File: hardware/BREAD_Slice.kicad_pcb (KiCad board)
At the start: 2 copper layers, 72.6 x 100 mm, 16 parts, among them J1 Conn_01x10_Female, J2 I2C_01x04

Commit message: Initial commit
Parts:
- removed C3, C4: 22uF, Capacitor_SMD:C_1206_3216Metric
- removed D1: WS2812B_5050, SparkFun-LED:WS2812-5050-4PIN
- removed HS1: Heatsink_Pad, SparkFun-Fuse:Thermal Pad
- removed J2: I2C_01x04, Connector_JST:JST_SH_SM04B-SRSS-TB_1x04-1MP_P1.00mm_Horizontal
- removed L1: 4.7uH, Inductor_SMD:L_1210_3225Metric
- removed U1: ~, Package_TO_SOT_SMD:TSOT-23-6
- C1: value 22uF -> 10uF_t; footprint Capacitor_SMD:C_1206_3216Metric -> OCI_UPL_FOOTPRINTS:C_2312
- C2: value 100nF -> 10uF_t; footprint Capacitor_SMD:C_1206_3216Metric -> OCI_UPL_FOOTPRINTS:C_2312
- H1, H4: footprint MountingHole:MountingHole_5mm -> MountingHole:MountingHole_3.2mm_M3_DIN965_Pad
- H2: renamed from H3; footprint MountingHole:MountingHole_5mm -> MountingHole:MountingHole_3.2mm_M3_DIN965_Pad
- H3: renamed from H2; footprint MountingHole:MountingHole_5mm -> MountingHole:MountingHole_3.2mm_M3_DIN965_Pad
- moved Logo1 77.4 mm to (171.3, 135.4), turned to 0 degrees
- moved C1 34.0 mm to (156.4, 100.0), turned to 0 degrees
- moved C2 31.4 mm to (156.4, 107.7), turned to 0 degrees
- moved A1 7.59 mm to (135.0, 100.0)
- moved J1 3.43 mm to (129.6, 78.8)
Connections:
- A1 pad 10: unconnected-(A1-D7-Pad10) -> /BR2
- A1 pad 11: unconnected-(A1-D8-Pad11) -> /THRM2
- A1 pad 12: unconnected-(A1-D9-Pad12) -> /DIR1
- A1 pad 13: unconnected-(A1-D10-Pad13) -> /MC1
- A1 pad 14: unconnected-(A1-D11-Pad14) -> /BR1
- A1 pad 15: unconnected-(A1-D12-Pad15) -> /THRM1
- A1 pad 19: unconnected-(A1-A0-Pad19) -> /A1
- A1 pad 20: unconnected-(A1-A1-Pad20) -> /B1
- A1 pad 21: unconnected-(A1-A2-Pad21) -> /A2
- A1 pad 22: unconnected-(A1-A3-Pad22) -> /B2
- A1 pad 25: unconnected-(A1-A6-Pad25) -> /CSEN1
- A1 pad 26: unconnected-(A1-A7-Pad26) -> /CSEN2
- A1 pad 30: unconnected-(A1-VIN-Pad30) -> +12V
- A1 pad 8: /LED -> /DIR2
- A1 pad 9: unconnected-(A1-D6-Pad9) -> /MC2
- C1 pad 1: GND -> +12V
- C1 pad 2: +12V -> GND
- C2 pad 1: Net-(U1-SW) -> +5V
- C2 pad 2: Net-(U1-BST) -> GND
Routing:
- net +5V: track 108.9 -> 3.60 mm, vias 1 -> 0
- net /LED: track 51.5 -> 0.00 mm
- net /I2C_CLK: track 78.5 -> 39.9 mm, vias 2 -> 1
- net /I2C_DAT: track 76.6 -> 39.9 mm, vias 2 -> 1
- net GND: track 19.6 -> 0.00 mm, vias 14 -> 0
- net /E_STOP: track 30.1 -> 20.9 mm
- net /INT: track 28.8 -> 20.9 mm
- net /SYNC: track 27.9 -> 20.9 mm
- net Net-(U1-SW): track 5.22 -> 0.00 mm
- net Net-(U1-BST): track 2.64 -> 0.00 mm
- net +12V: track 46.8 -> 45.5 mm
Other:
- board size 72.6 x 100 mm -> 70 x 100 mm
- board text added: "<Description> SLC_TEMP R<version#> year"
- board text removed: "12V->5V Reg"
- board text removed: "5V I2C Connector"
- board text removed: "BREAD Slice Template SLC_TEMP <version> <year>"
- board text removed: "LED"

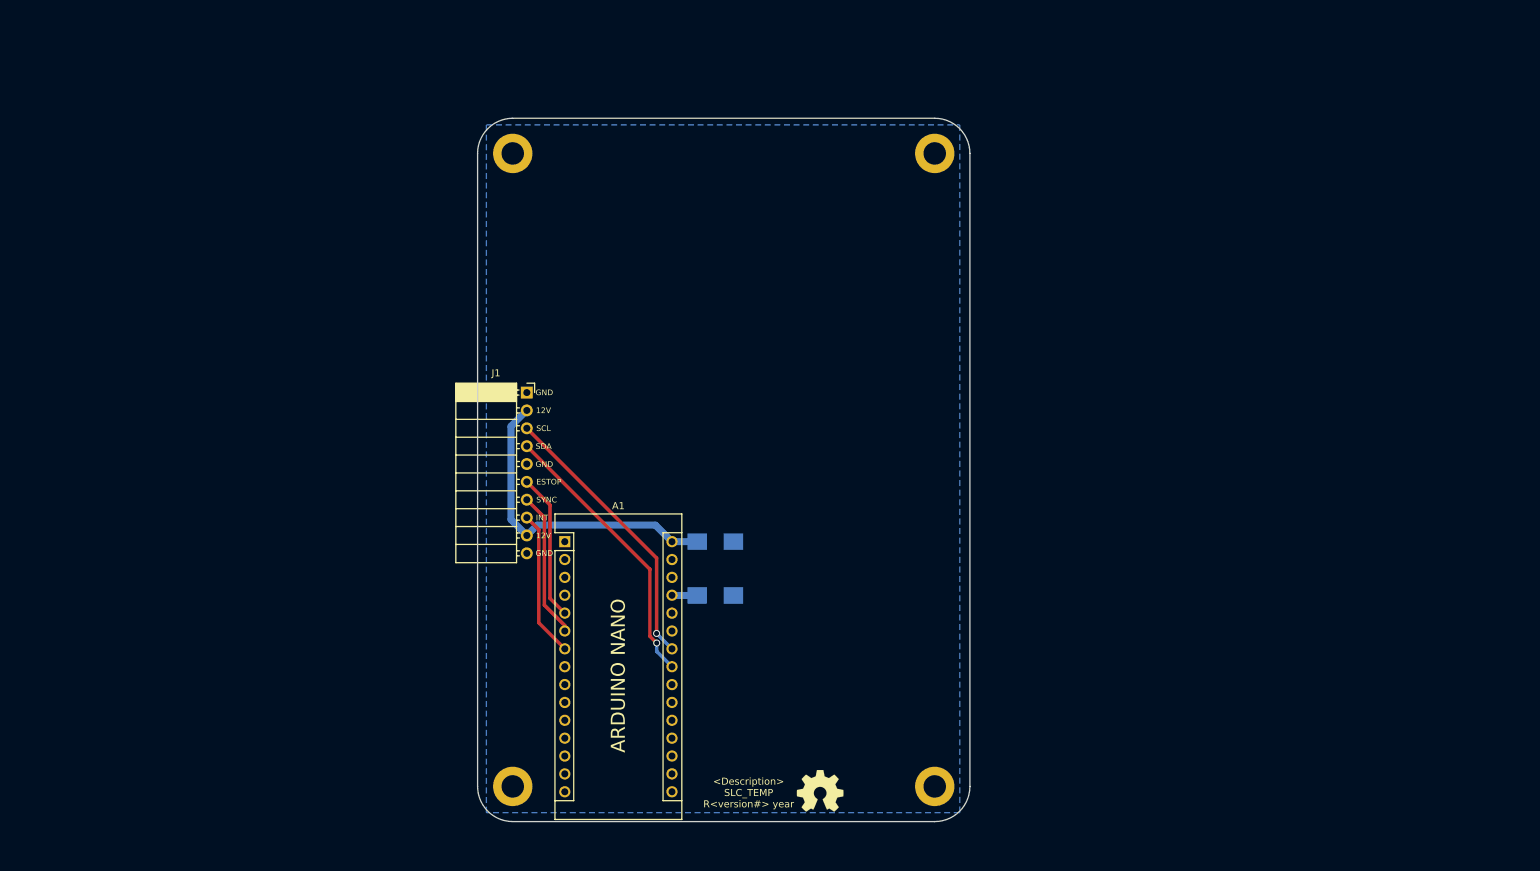
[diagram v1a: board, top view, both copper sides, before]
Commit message: initial layout poisitions done
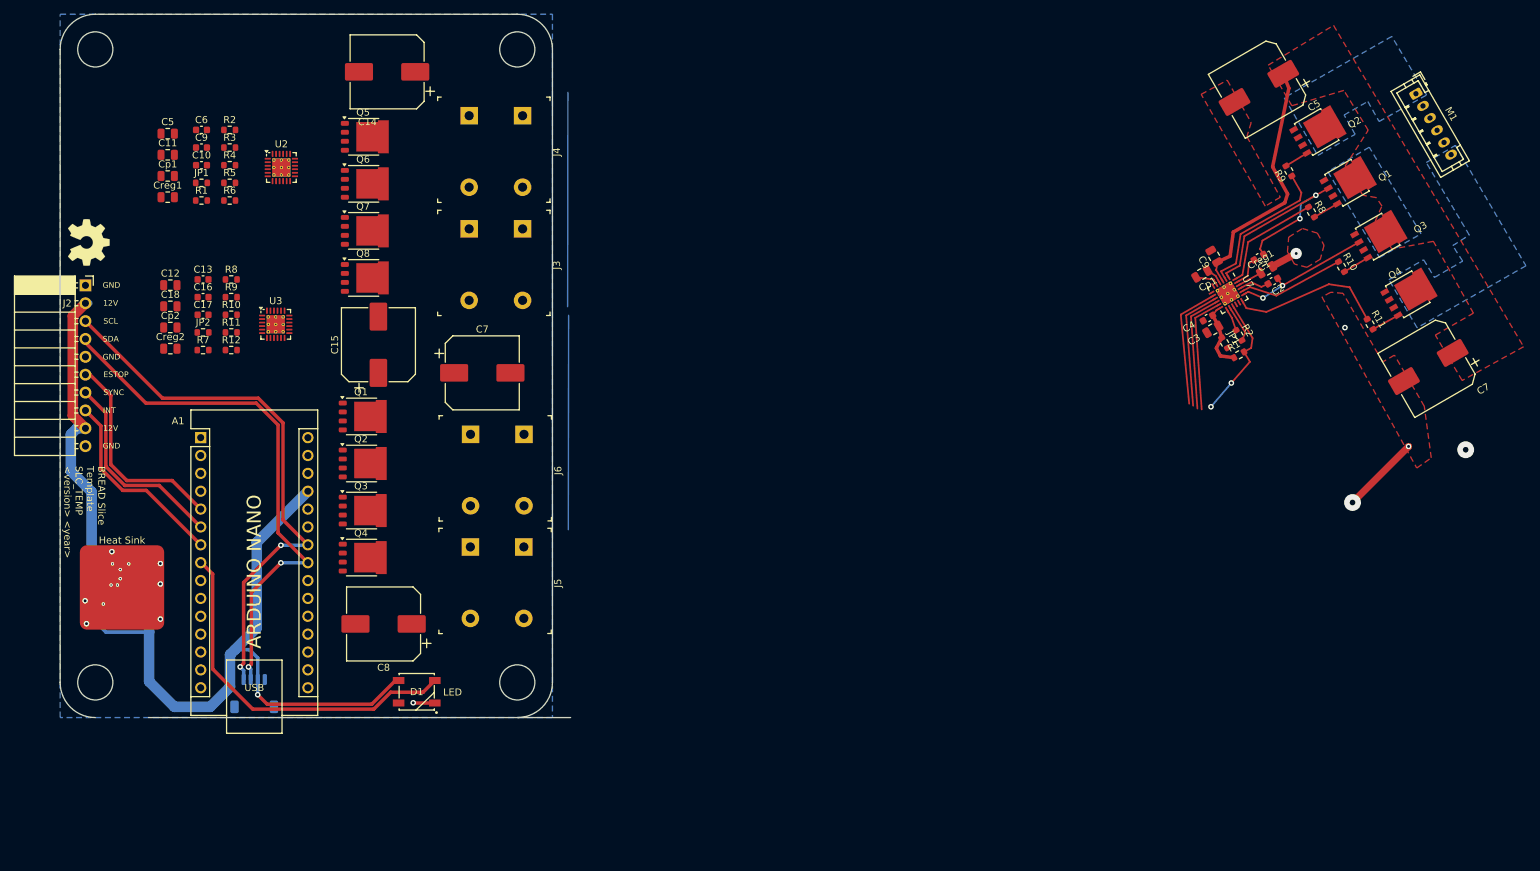
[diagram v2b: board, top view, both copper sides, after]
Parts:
- removed the C1 at (156.4, 100.0)
- removed the C2 at (156.4, 107.7)
- added C1: 10n, Capacitor_SMD:C_0603_1608Metric, F.Cu at (233.7, 59.6)
- added C1: 22uF, Capacitor_SMD:C_1206_3216Metric, B.Cu at (69.2, 104.7)
- added C10: 1n, Capacitor_SMD:C_0603_1608Metric, F.Cu at (83.3, 46.5)
- added C11: 50V 10U, Capacitor_SMD:C_0805_2012Metric, F.Cu at (78.5, 45.0)
- added C12: 10U, Capacitor_SMD:C_0805_2012Metric, F.Cu at (78.9, 63.5)
- added C13: 100N, Capacitor_SMD:C_0603_1608Metric, F.Cu at (83.6, 62.7)
- added C14: 50V 220U, Capacitor_SMD:CP_Elec_10x10, F.Cu at (109.7, 33.2)
- added C15: 50V 220U, Capacitor_SMD:CP_Elec_10x10, F.Cu at (108.5, 72.0)
- added C16: 1n, Capacitor_SMD:C_0603_1608Metric, F.Cu at (83.6, 65.2)
- added C17: 1n, Capacitor_SMD:C_0603_1608Metric, F.Cu at (83.6, 67.7)
- added C18: 50V 10U, Capacitor_SMD:C_0805_2012Metric, F.Cu at (78.9, 66.5)
- added C2: 10n, Capacitor_SMD:C_0603_1608Metric, F.Cu at (235.7, 63.0)
- added C2: 100nF, Capacitor_SMD:C_1206_3216Metric, B.Cu at (71.8, 111.5)
- added C3: 10U, Capacitor_SMD:C_0805_2012Metric, F.Cu at (227.1, 69.8)
- added C3: 22uF, Capacitor_SMD:C_1206_3216Metric, B.Cu at (74.5, 104.7)
- added C4: 100N, Capacitor_SMD:C_0603_1608Metric, F.Cu at (226.4, 68.2)
- added C4: 22uF, Capacitor_SMD:C_1206_3216Metric, B.Cu at (74.5, 101.7)
- added C5: 50V 220U, Capacitor_SMD:CP_Elec_10x10, F.Cu at (233.7, 35.5)
- added C5: 10U, Capacitor_SMD:C_0805_2012Metric, F.Cu at (78.5, 42.0)
- added C6: 100N, Capacitor_SMD:C_0603_1608Metric, F.Cu at (83.3, 41.5)
- added C7: 50V 220U, Capacitor_SMD:CP_Elec_10x10, F.Cu at (123.3, 76.0)
- added C7: 50V 220U, Capacitor_SMD:CP_Elec_10x10, F.Cu at (257.8, 75.2)
- added C8: 50V 220U, Capacitor_SMD:CP_Elec_10x10, F.Cu at (109.2, 111.7)
- added C9: 50V 10U, Capacitor_SMD:C_0805_2012Metric, F.Cu at (227.3, 59.4)
- added C9: 1n, Capacitor_SMD:C_0603_1608Metric, F.Cu at (83.3, 44.0)
- added Cp1: 16V 470n, Capacitor_SMD:C_0805_2012Metric, F.Cu at (225.6, 61.9)
- added Cp1: 16V 470n, Capacitor_SMD:C_0805_2012Metric, F.Cu at (78.5, 48.0)
- added Cp2: 16V 470n, Capacitor_SMD:C_0805_2012Metric, F.Cu at (78.9, 69.5)
- added Creg1: 16V 22u, Capacitor_SMD:C_0805_2012Metric, F.Cu at (234.8, 61.3)
- added Creg1: 16V 22u, Capacitor_SMD:C_0805_2012Metric, F.Cu at (78.5, 51.0)
- added Creg2: 16V 22u, Capacitor_SMD:C_0805_2012Metric, F.Cu at (78.9, 72.6)
- added D1: WS2812B_5050, SparkFun-LED:WS2812-5050-4PIN, F.Cu at (113.9, 121.3)
- added HS1: Heatsink_Pad, KML-Custom:Thermal Pad, F.Cu at (72.0, 106.5)
- added J1: I2C_01x04, Connector_JST:JST_SH_SM04B-SRSS-TB_1x04-1MP_P1.00mm_Horizontal, B.Cu at (90.8, 121.6)
- added J3: Conn_01x02_Socket, Library:Term_Block_1x2_P10.16mm, F.Cu at (129.0, 55.5)
- added J4: Conn_01x02_Socket, Library:Term_Block_1x2_P10.16mm, F.Cu at (129.0, 39.4)
- added J5: Conn_01x02_Socket, Library:Term_Block_1x2_P10.16mm, F.Cu at (129.2, 100.8)
- added J6: Conn_01x02_Socket, Library:Term_Block_1x2_P10.16mm, F.Cu at (129.2, 84.7)
- added JP1: Jumper_2_Open, Resistor_SMD:R_0603_1608Metric, F.Cu at (83.3, 49.0)
- added JP1: Jumper_2_Open, Resistor_SMD:R_0603_1608Metric, F.Cu at (228.8, 71.7)
- added JP2: Jumper_2_Open, Resistor_SMD:R_0603_1608Metric, F.Cu at (83.6, 70.2)
- added L1: 4.7uH, Inductor_SMD:L_1210_3225Metric, B.Cu at (74.5, 108.0)
- added M1: Motor_2BitEncoder, Connector_JST:JST_PH_B6B-PH-K_1x06_P2.00mm_Vertical, F.Cu at (256.0, 36.3)
- added Q1: PSMN1R0-30YLC,115, Package_TO_SOT_SMD:LFPAK56, F.Cu at (106.1, 82.2)
- added Q1: PSMN1R0-30YLC,115, Package_TO_SOT_SMD:LFPAK56, F.Cu at (246.2, 49.0)
- added Q2: PSMN1R0-30YLC,115, Package_TO_SOT_SMD:LFPAK56, F.Cu at (241.9, 41.8)
- added Q2: PSMN1R0-30YLC,115, Package_TO_SOT_SMD:LFPAK56, F.Cu at (106.1, 88.9)
- added Q3: PSMN1R0-30YLC,115, Package_TO_SOT_SMD:LFPAK56, F.Cu at (106.1, 95.6)
- added Q3: PSMN1R0-30YLC,115, Package_TO_SOT_SMD:LFPAK56, F.Cu at (250.6, 56.6)
- added Q4: PSMN1R0-30YLC,115, Package_TO_SOT_SMD:LFPAK56, F.Cu at (106.1, 102.3)
- added Q4: PSMN1R0-30YLC,115, Package_TO_SOT_SMD:LFPAK56, F.Cu at (254.9, 64.8)
- added Q5: PSMN1R0-30YLC,115, Package_TO_SOT_SMD:LFPAK56, F.Cu at (106.4, 42.4)
- added Q6: PSMN1R0-30YLC,115, Package_TO_SOT_SMD:LFPAK56, F.Cu at (106.4, 49.1)
- added Q7: PSMN1R0-30YLC,115, Package_TO_SOT_SMD:LFPAK56, F.Cu at (106.4, 55.8)
- added Q8: PSMN1R0-30YLC,115, Package_TO_SOT_SMD:LFPAK56, F.Cu at (106.4, 62.5)
- added R1: 10K, Resistor_SMD:R_0603_1608Metric, F.Cu at (230.9, 73.4)
- added R1: 10K, Resistor_SMD:R_0603_1608Metric, F.Cu at (83.3, 51.5)
- added R10: 1K, Resistor_SMD:R_0603_1608Metric, F.Cu at (87.6, 67.7)
- added R10: 1K, Resistor_SMD:R_0603_1608Metric, F.Cu at (245.4, 60.9)
- added R11: 1K, Resistor_SMD:R_0603_1608Metric, F.Cu at (249.5, 69.1)
- added R11: 1K, Resistor_SMD:R_0603_1608Metric, F.Cu at (87.6, 70.2)
- added R12: 10K, Resistor_SMD:R_0603_1608Metric, F.Cu at (87.6, 72.8)
- added R2: 1K, Resistor_SMD:R_0603_1608Metric, F.Cu at (87.4, 41.5)
- added R2: 10K, Resistor_SMD:R_0603_1608Metric, F.Cu at (230.9, 70.7)
- added R3: 1K, Resistor_SMD:R_0603_1608Metric, F.Cu at (87.4, 44.0)
- added R4: 1K, Resistor_SMD:R_0603_1608Metric, F.Cu at (87.4, 46.5)
- added R5: 1K, Resistor_SMD:R_0603_1608Metric, F.Cu at (87.4, 49.0)
- added R6: 10K, Resistor_SMD:R_0603_1608Metric, F.Cu at (87.4, 51.5)
- added R7: 10K, Resistor_SMD:R_0603_1608Metric, F.Cu at (83.6, 72.8)
- added R8: 1K, Resistor_SMD:R_0603_1608Metric, F.Cu at (241.2, 53.1)
- added R8: 1K, Resistor_SMD:R_0603_1608Metric, F.Cu at (87.6, 62.7)
- added R9: 1K, Resistor_SMD:R_0603_1608Metric, F.Cu at (87.6, 65.2)
- added R9: 1K, Resistor_SMD:R_0603_1608Metric, F.Cu at (238.0, 47.3)
- added U1: ~, Package_TO_SOT_SMD:TSOT-23-6, B.Cu at (69.4, 108.0)
- added U2: ~, Package_DFN_QFN:HVQFN-24-1EP_4x4mm_P0.5mm_EP2.6x2.6mm_ThermalVias, F.Cu at (94.7, 46.8)
- added U3: ~, Package_DFN_QFN:HVQFN-24-1EP_4x4mm_P0.5mm_EP2.6x2.6mm_ThermalVias, F.Cu at (93.9, 69.1)
- added U7: ~, Package_DFN_QFN:HVQFN-24-1EP_4x4mm_P0.5mm_EP2.6x2.6mm_ThermalVias, F.Cu at (229.3, 64.7)
- H1, H4: footprint MountingHole:MountingHole_3.2mm_M3_DIN965_Pad -> MountingHole:MountingHole_5mm
- H2: renamed from H3; footprint MountingHole:MountingHole_3.2mm_M3_DIN965_Pad -> MountingHole:MountingHole_5mm
- H3: renamed from H2; footprint MountingHole:MountingHole_3.2mm_M3_DIN965_Pad -> MountingHole:MountingHole_5mm
- moved Logo1 130.0 mm to (67.3, 57.4), turned to -90 degrees
- moved J2 64.6 mm to (66.8, 63.6)
- moved H1 61.2 mm to (68.2, 30.0)
- moved H2 61.2 mm to (68.2, 120.0)
- moved H3 61.2 mm to (128.2, 30.0)
- moved H4 61.2 mm to (128.2, 120.0)
- moved A1 53.8 mm to (83.2, 85.2)
- renumbered J1 to J2
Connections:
- A1 pad 10: /BR2 -> /BLO1
- A1 pad 11: /THRM2 -> /AHI1
- A1 pad 12: /DIR1 -> /ALO1
- A1 pad 13: /MC1 -> /BHI2
- A1 pad 14: /BR1 -> /BLO2
- A1 pad 15: /THRM1 -> /AHI2
- A1 pad 16: unconnected-(A1-Pad16) -> /ALO2
- A1 pad 19: /A1 -> /FAULT1
- A1 pad 20: /B1 -> /RESET1
- A1 pad 21: /A2 -> /FAULT2
- A1 pad 22: /B2 -> /RESET2
- A1 pad 25: /CSEN1 -> unconnected-(A1-A6-Pad25)
- A1 pad 26: /CSEN2 -> unconnected-(A1-A7-Pad26)
- A1 pad 30: +12V -> unconnected-(A1-VIN-Pad30)
- A1 pad 8: /DIR2 -> /LED
- A1 pad 9: /MC2 -> /BHI1
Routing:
- net (no net): track 0.00 -> 290.5 mm, vias 0 -> 7
- net +5V: track 3.60 -> 116.8 mm, vias 0 -> 1
- net /LED: track 0.00 -> 51.5 mm
- net /I2C_CLK: track 39.9 -> 78.5 mm, vias 1 -> 2
- net GND: track 0.00 -> 37.9 mm, vias 0 -> 18
- net /I2C_DAT: track 39.9 -> 76.6 mm, vias 1 -> 2
- net /E_STOP: track 20.9 -> 30.1 mm
- net /INT: track 20.9 -> 28.8 mm
- net /SYNC: track 20.9 -> 27.9 mm
- net Net-(U1-SW): track 0.00 -> 5.22 mm
- net Net-(U1-BST): track 0.00 -> 2.64 mm
- net +12V: track 45.5 -> 46.8 mm
- added copper zone on B.Cu, net (none)
- added copper zone on F.Cu, net (none)
- added copper zone on F.Cu, net GND
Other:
- board size 70 x 100 mm -> 72.6 x 100 mm
- board text added: "12V->5V Reg"
- board text added: "5V I2C Connector"
- board text added: "BREAD Slice Template SLC_TEMP <version> <year>"
- board text added: "LED"
- board text removed: "<Description> SLC_TEMP R<version#> year"

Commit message: set repo
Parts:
- removed the C1 at (233.7, 59.6)
- removed the C2 at (235.7, 63.0)
- removed the C3 at (227.1, 69.8)
- removed the C4 at (226.4, 68.2)
- removed the C5 at (233.7, 35.5)
- removed the C7 at (257.8, 75.2)
- removed the C9 at (227.3, 59.4)
- removed the C9 at (83.3, 44.0)
- removed the Cp1 at (225.6, 61.9)
- removed the Creg1 at (234.8, 61.3)
- removed the JP1 at (83.3, 49.0)
- removed the JP1 at (228.8, 71.7)
- removed M1: Motor_2BitEncoder, Connector_JST:JST_PH_B6B-PH-K_1x06_P2.00mm_Vertical
- removed the Q1 at (246.2, 49.0)
- removed the Q2 at (241.9, 41.8)
- removed the Q3 at (250.6, 56.6)
- removed the Q4 at (254.9, 64.8)
- removed the R1 at (230.9, 73.4)
- removed the R1 at (83.3, 51.5)
- removed the R10 at (87.6, 67.7)
- removed the R10 at (245.4, 60.9)
- removed the R11 at (249.5, 69.1)
- removed the R11 at (87.6, 70.2)
- removed the R2 at (87.4, 41.5)
- removed the R2 at (230.9, 70.7)
- removed the R8 at (241.2, 53.1)
- removed the R8 at (87.6, 62.7)
- removed the R9 at (87.6, 65.2)
- removed the R9 at (238.0, 47.3)
- removed U7: ~, Package_DFN_QFN:HVQFN-24-1EP_4x4mm_P0.5mm_EP2.6x2.6mm_ThermalVias
- added C9: 1nF, Capacitor_SMD:C_0805_2012Metric, F.Cu at (99.6, 44.9)
- added JP1: Jumper_2_Open, Capacitor_SMD:C_0805_2012Metric, F.Cu at (91.4, 52.8)
- added R1: 10K, Capacitor_SMD:C_0805_2012Metric, F.Cu at (91.4, 54.8)
- added R10: 1K, Capacitor_SMD:C_0805_2012Metric, F.Cu at (102.3, 98.3)
- added R11: 1K, Capacitor_SMD:C_0805_2012Metric, F.Cu at (103.2, 105.7)
- added R2: 1K, Capacitor_SMD:C_0805_2012Metric, F.Cu at (103.2, 51.4)
- added R8: 1K, Capacitor_SMD:C_0805_2012Metric, F.Cu at (103.5, 92.4)
- added R9: 1K, Capacitor_SMD:C_0805_2012Metric, F.Cu at (103.5, 84.7)
- C10, C16, C17: value 1n -> 1nF; footprint Capacitor_SMD:C_0603_1608Metric -> Capacitor_SMD:C_0805_2012Metric
- C11, C18: value 50V 10U -> 50V 10uF
- C12, C5: value 10U -> 10uF
- C13, C6: value 100N -> 100nF; footprint Capacitor_SMD:C_0603_1608Metric -> Capacitor_SMD:C_0805_2012Metric
- C14, C15, C7, C8: value 50V 220U -> 50V 220uF
- Cp1, Cp2: value 16V 470n -> 16V 470nF
- Creg1, Creg2: value 16V 22u -> 16V 22uF
- JP2, R12, R3, R4, R5, R6, R7: footprint Resistor_SMD:R_0603_1608Metric -> Capacitor_SMD:C_0805_2012Metric
- moved Q5 48.2 mm to (108.9, 90.5)
- moved Q2 47.5 mm to (108.8, 41.4)
- moved C7 46.1 mm to (107.4, 32.8), turned to 180 degrees
- moved C14 43.8 mm to (122.2, 75.2), turned to -90 degrees
- moved Q8 41.5 mm to (108.8, 103.9)
- moved C15 40.7 mm to (108.4, 112.7), turned to 180 degrees
- moved Q7 40.5 mm to (108.9, 96.2)
- moved Q3 40.5 mm to (108.9, 55.2)
- moved Q4 39.3 mm to (108.8, 63.0)
- moved C8 38.6 mm to (110.8, 73.2), turned to -90 degrees
- moved Q6 33.7 mm to (108.8, 82.8)
- moved Q1 32.7 mm to (108.9, 49.6)
- moved R5 22.5 mm to (103.2, 65.0)
- moved Creg1 21.6 mm to (99.7, 46.9)
- moved Creg2 20.8 mm to (99.4, 69.1)
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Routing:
- net (no net): track 290.5 -> 0.00 mm, vias 7 -> 0
- net /A4947 H-Bridge1/VBB: track 0.00 -> 97.3 mm, vias 0 -> 2
- net /A4947 H-Bridge/VBB: track 0.00 -> 81.3 mm, vias 0 -> 5
- net /A4947 H-Bridge1/SB: track 0.00 -> 79.6 mm, vias 0 -> 2
- net /ALO1: track 0.00 -> 77.0 mm, vias 0 -> 1
- net /FAULT1: track 0.00 -> 73.5 mm, vias 0 -> 3
- net /AHI1: track 0.00 -> 73.0 mm, vias 0 -> 1
- net /BLO1: track 0.00 -> 72.7 mm, vias 0 -> 1
- net /RESET1: track 0.00 -> 70.3 mm, vias 0 -> 3
- net /BHI1: track 0.00 -> 68.4 mm, vias 0 -> 1
- net /ALO2: track 0.00 -> 59.7 mm, vias 0 -> 4
- net /BLO2: track 0.00 -> 57.5 mm, vias 0 -> 1
- net /A4947 H-Bridge/SB: track 0.00 -> 55.8 mm, vias 0 -> 2
- net /A4947 H-Bridge1/SA: track 0.00 -> 54.8 mm, vias 0 -> 3
- net /BHI2: track 0.00 -> 53.6 mm, vias 0 -> 4
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- removed copper zone on B.Cu, net (none)
- removed copper zone on F.Cu, net (none)
- removed copper zone on F.Cu, net GND
